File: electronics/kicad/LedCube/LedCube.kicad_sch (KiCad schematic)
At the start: 24 parts, among them J1 Conn_01x03, J2 Conn_01x03, J3 Conn_01x03, J4 Conn_01x04, J5 COM, J6 Conn_01x02, J7 JTAG, U3 ESP32-DevKitM

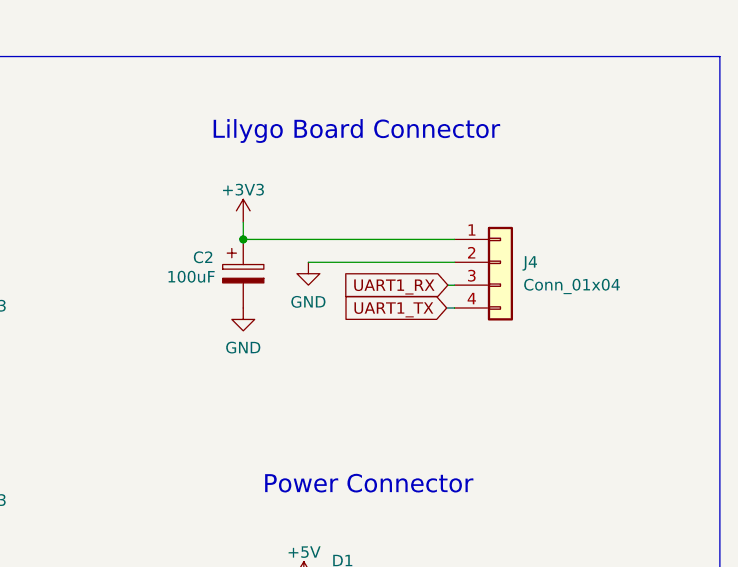
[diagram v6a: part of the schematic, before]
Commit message: Fix flipped vcc and gnd in KiCad
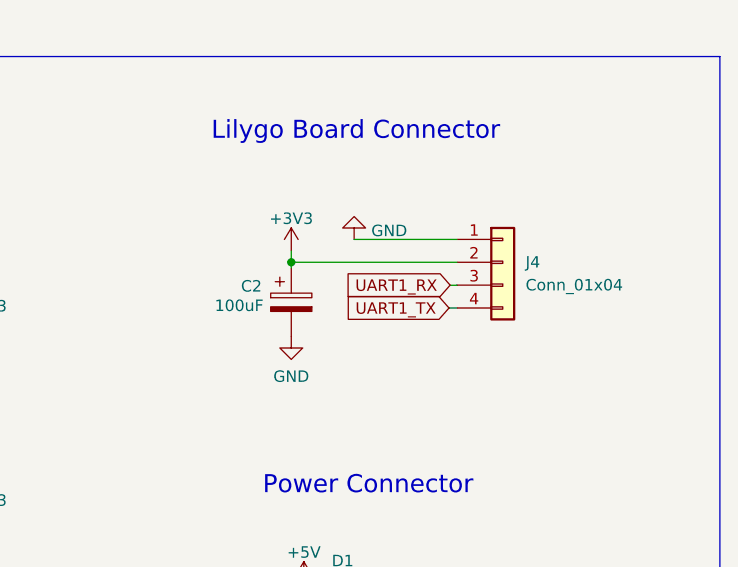
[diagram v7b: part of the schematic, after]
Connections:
- net +3V3: now also J4.2 (Pin_2); no longer J4.1 (Pin_1)
- net GND: now also J4.1 (Pin_1); no longer J4.2 (Pin_2)
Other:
- moved on the sheet: C2
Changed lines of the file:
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@@
   (junction (at 224.155 52.705) (diameter 0) (color 0 0 0 0)
   )
-  (junction (at 225.171 98.425) (diameter 0) (color 0 0 0 0)
+  (junction (at 230.505 100.965) (diameter 0) (color 0 0 0 0)
   )
   (no_connect (at 240.665 55.245))
@@
     (stroke (width 0) (type default))
   )
-  (wire (pts (xy 247.777 106.045) (xy 248.666 106.045))
+  (wire (pts (xy 248.031 106.045) (xy 248.92 106.045))
     (stroke (width 0) (type default))
   )
@@
     (stroke (width 0) (type default))
   )
-  (wire (pts (xy 232.41 100.965) (xy 248.666 100.965))
-    (stroke (width 0) (type default))
-  )
   (wire (pts (xy 175.895 132.08) (xy 180.975 132.08))
     (stroke (width 0) (type default))
   )
-  (wire (pts (xy 225.171 96.52) (xy 225.171 98.425))
+  (wire (pts (xy 230.505 99.695) (xy 230.505 100.965))
     (stroke (width 0) (type default))
   )
@@
     (stroke (width 0) (type default))
   )
-  (wire (pts (xy 247.904 103.505) (xy 248.666 103.505))
+  (wire (pts (xy 248.158 103.505) (xy 248.92 103.505))
     (stroke (width 0) (type default))
   )
@@
     (stroke (width 0) (type default))
   )
-  (wire (pts (xy 248.666 98.425) (xy 225.171 98.425))
+  (wire (pts (xy 230.505 100.965) (xy 230.505 101.6))
+    (stroke (width 0) (type default))
+  )
+  (wire (pts (xy 230.505 100.965) (xy 248.92 100.965))
     (stroke (width 0) (type default))
   )
@@
   )
   (wire (pts (xy 224.155 52.705) (xy 227.965 52.705))
+    (stroke (width 0) (type default))
+  )
+  (wire (pts (xy 237.49 98.425) (xy 248.92 98.425))
     (stroke (width 0) (type default))
   )
@@
     )
   )
-  (global_label "UART1_RX" (shape input) (at 247.904 103.505 180) (fields_autoplaced)
-    (effects (font (size 1.27 1.27)) (justify right))
-    (property "Intersheetrefs" "${INTERSHEET_REFS}" (at 236.1776 103.4256 0)
+  (global_label "UART1_RX" (shape input) (at 248.158 103.505 180) (fields_autoplaced)
+    (effects (font (size 1.27 1.27)) (justify right))
+    (property "Intersheetrefs" "${INTERSHEET_REFS}" (at 236.4316 103.4256 0)
       (effects (font (size 1.27 1.27)) (justify right) hide)
     )
@@
     )
   )
-  (global_label "UART1_TX" (shape input) (at 247.777 106.045 180) (fields_autoplaced)
-    (effects (font (size 1.27 1.27)) (justify right))
-    (property "Intersheetrefs" "${INTERSHEET_REFS}" (at 236.3529 105.9656 0)
+  (global_label "UART1_TX" (shape input) (at 248.031 106.045 180) (fields_autoplaced)
+    (effects (font (size 1.27 1.27)) (justify right))
+    (property "Intersheetrefs" "${INTERSHEET_REFS}" (at 236.6069 105.9656 0)
       (effects (font (size 1.27 1.27)) (justify right) hide)
     )
@@
     )
   )
-  (symbol (lib_id "Device:C_Polarized") (at 225.171 102.235 0) (unit 1)
+  (symbol (lib_id "Device:C_Polarized") (at 230.505 105.41 0) (unit 1)
     (in_bom yes) (on_board yes) (dnp no)
-    (property "Reference" "C2" (at 219.583 100.457 0)
-      (effects (font (size 1.27 1.27)) (justify left))
-    )
-    (property "Value" "100uF" (at 216.662 102.616 0)
-      (effects (font (size 1.27 1.27)) (justify left))
-    )
-    (property "Footprint" "Capacitor_THT:C_Radial_D5.0mm_H5.0mm_P2.00mm" (at 226.1362 106.045 0)
-      (effects (font (size 1.27 1.27)) hide)
-    )
-    (property "Datasheet" "~" (at 225.171 102.235 0)
+    (property "Reference" "C2" (at 224.917 103.632 0)
+      (effects (font (size 1.27 1.27)) (justify left))
+    )
+    (property "Value" "100uF" (at 221.996 105.791 0)
+      (effects (font (size 1.27 1.27)) (justify left))
+    )
+    (property "Footprint" "Capacitor_THT:C_Radial_D5.0mm_H5.0mm_P2.00mm" (at 231.4702 109.22 0)
+      (effects (font (size 1.27 1.27)) hide)
+    )
+    (property "Datasheet" "~" (at 230.505 105.41 0)
       (effects (font (size 1.27 1.27)) hide)
     )
@@
     )
   )
-  (symbol (lib_id "power:+3V3") (at 225.171 96.52 0) (unit 1)
-    (in_bom yes) (on_board yes) (dnp no) (fields_autoplaced)
-    (property "Reference" "#PWR0108" (at 225.171 100.33 0)
-      (effects (font (size 1.27 1.27)) hide)
-    )
-    (property "Value" "+3V3" (at 225.171 92.9442 0)
-      (effects (font (size 1.27 1.27)))
-    )
-    (property "Footprint" "" (at 225.171 96.52 0)
-      (effects (font (size 1.27 1.27)) hide)
-    )
-    (property "Datasheet" "" (at 225.171 96.52 0)
+  (symbol (lib_id "power:+3V3") (at 230.505 99.695 0) (unit 1)
+    (in_bom yes) (on_board yes) (dnp no) (fields_autoplaced)
+    (property "Reference" "#PWR0108" (at 230.505 103.505 0)
+      (effects (font (size 1.27 1.27)) hide)
+    )
+    (property "Value" "+3V3" (at 230.505 96.1192 0)
+      (effects (font (size 1.27 1.27)))
+    )
+    (property "Footprint" "" (at 230.505 99.695 0)
+      (effects (font (size 1.27 1.27)) hide)
+    )
+    (property "Datasheet" "" (at 230.505 99.695 0)
       (effects (font (size 1.27 1.27)) hide)
     )
@@
     )
   )
-  (symbol (lib_id "power:GND") (at 225.171 106.045 0) (unit 1)
-    (in_bom yes) (on_board yes) (dnp no) (fields_autoplaced)
-    (property "Reference" "#PWR07" (at 225.171 112.395 0)
-      (effects (font (size 1.27 1.27)) hide)
-    )
-    (property "Value" "GND" (at 225.171 110.4884 0)
-      (effects (font (size 1.27 1.27)))
-    )
-    (property "Footprint" "" (at 225.171 106.045 0)
-      (effects (font (size 1.27 1.27)) hide)
-    )
-    (property "Datasheet" "" (at 225.171 106.045 0)
+  (symbol (lib_id "power:GND") (at 230.505 109.22 0) (unit 1)
+    (in_bom yes) (on_board yes) (dnp no) (fields_autoplaced)
+    (property "Reference" "#PWR07" (at 230.505 115.57 0)
+      (effects (font (size 1.27 1.27)) hide)
+    )
+    (property "Value" "GND" (at 230.505 113.6634 0)
+      (effects (font (size 1.27 1.27)))
+    )
+    (property "Footprint" "" (at 230.505 109.22 0)
+      (effects (font (size 1.27 1.27)) hide)
+    )
+    (property "Datasheet" "" (at 230.505 109.22 0)
       (effects (font (size 1.27 1.27)) hide)
     )
@@
     )
   )
-  (symbol (lib_id "power:GND") (at 232.41 100.965 0) (unit 1)
-    (in_bom yes) (on_board yes) (dnp no) (fields_autoplaced)
-    (property "Reference" "#PWR0109" (at 232.41 107.315 0)
-      (effects (font (size 1.27 1.27)) hide)
-    )
-    (property "Value" "GND" (at 232.41 105.4084 0)
-      (effects (font (size 1.27 1.27)))
-    )
-    (property "Footprint" "" (at 232.41 100.965 0)
-      (effects (font (size 1.27 1.27)) hide)
-    )
-    (property "Datasheet" "" (at 232.41 100.965 0)
+  (symbol (lib_id "power:GND") (at 237.49 98.425 180) (unit 1)
+    (in_bom yes) (on_board yes) (dnp no) (fields_autoplaced)
+    (property "Reference" "#PWR0109" (at 237.49 92.075 0)
+      (effects (font (size 1.27 1.27)) hide)
+    )
+    (property "Value" "GND" (at 239.395 97.4718 0)
+      (effects (font (size 1.27 1.27)) (justify right))
+    )
+    (property "Footprint" "" (at 237.49 98.425 0)
+      (effects (font (size 1.27 1.27)) hide)
+    )
+    (property "Datasheet" "" (at 237.49 98.425 0)
       (effects (font (size 1.27 1.27)) hide)
     )
@@
     )
   )
-  (symbol (lib_id "Connector_Generic:Conn_01x04") (at 253.746 100.965 0) (unit 1)
-    (in_bom yes) (on_board yes) (dnp no) (fields_autoplaced)
-    (property "Reference" "J4" (at 256.286 100.9649 0)
-      (effects (font (size 1.27 1.27)) (justify left))
-    )
-    (property "Value" "Conn_01x04" (at 256.286 103.5049 0)
-      (effects (font (size 1.27 1.27)) (justify left))
-    )
-    (property "Footprint" "Connectors:Grove_1x04" (at 253.746 100.965 0)
-      (effects (font (size 1.27 1.27)) hide)
-    )
-    (property "Datasheet" "~" (at 253.746 100.965 0)
-      (effects (font (size 1.27 1.27)) hide)
-    )
+  (symbol (lib_id "Connector_Generic:Conn_01x04") (at 254 100.965 0) (unit 1)
+    (in_bom yes) (on_board yes) (dnp no) (fields_autoplaced)
+    (property "Reference" "J4" (at 256.54 100.9649 0)
+      (effects (font (size 1.27 1.27)) (justify left))
+    )
+    (property "Value" "Conn_01x04" (at 256.54 103.5049 0)
+      (effects (font (size 1.27 1.27)) (justify left))
+    )
+    (property "Footprint" "Connectors:Grove_1x04" (at 254 100.965 0)
+      (effects (font (size 1.27 1.27)) hide)
+    )
+    (property "Datasheet" "~" (at 254 100.965 0)
+      (effects (font (size 1.27 1.27)) hide)
+    )
